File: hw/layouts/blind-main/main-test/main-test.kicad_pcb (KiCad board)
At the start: 2 copper layers, 191 parts

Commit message: Place compact controller and capture split battery carriers
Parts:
- added D6: , blind-control-io:SOT-553-5_L1.6-W1.2-P0.50-LS1.6-TL-1, F.Cu at (135.8, 130.5)
- added J2: , blind-harness:CONN-SMD_4P-P1.25_53261-0471, F.Cu at (140.0, 131.5)
- added J3: , blind-harness:CONN-TH_532610371, F.Cu at (130.5, 123.0)
- added TP1: , blind-pack-features:WirePad18, F.Cu at (142.0, 140.5)
- added TP2: , blind-pack-features:WirePad18, F.Cu at (148.0, 140.5)
- moved C45 1303.6 mm to (112.6, 127.2)
- moved C44 1294.7 mm to (112.3, 134.6)
- moved C41 1282.3 mm to (105.0, 137.0)
- moved C43 1280.6 mm to (116.5, 135.5), turned to 90 degrees
- moved C40 1260.9 mm to (116.0, 132.0)
- moved C42 1253.8 mm to (112.9, 129.3)
- moved L2 1250.0 mm to (107.0, 132.0)
- moved C46 1238.5 mm to (109.0, 135.5)
- moved R46 1227.8 mm to (108.9, 128.5)
- moved R45 1221.1 mm to (105.5, 127.0)
- moved R44 1212.7 mm to (104.2, 128.5)
- moved U9 1195.3 mm to (112.0, 132.0)
- moved C2 1163.4 mm to (137.3, 157.2), turned to 90 degrees
- moved C1 1156.1 mm to (134.6, 157.2), turned to 90 degrees
- moved C21 1131.4 mm to (147.9, 145.1), turned to 90 degrees
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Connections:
- net encoder_a_raw renamed channel_a
- net encoder_b_raw renamed channel_b
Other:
- board outline added: 54 x 71 mm
- copper layers 2 -> 4
- board text added: "SB-C1 R0"

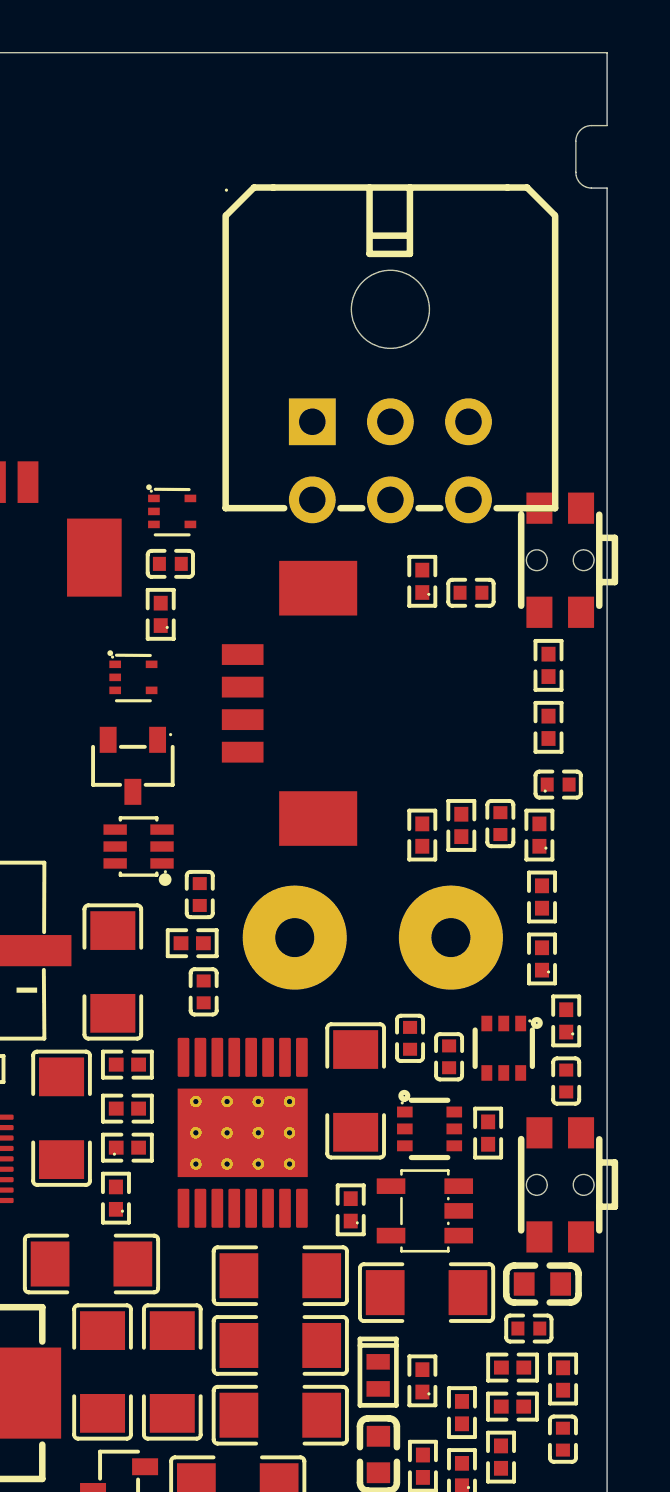
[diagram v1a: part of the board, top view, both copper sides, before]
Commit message: Coordinate retained enclosure and PCB clearance repair checkpoint
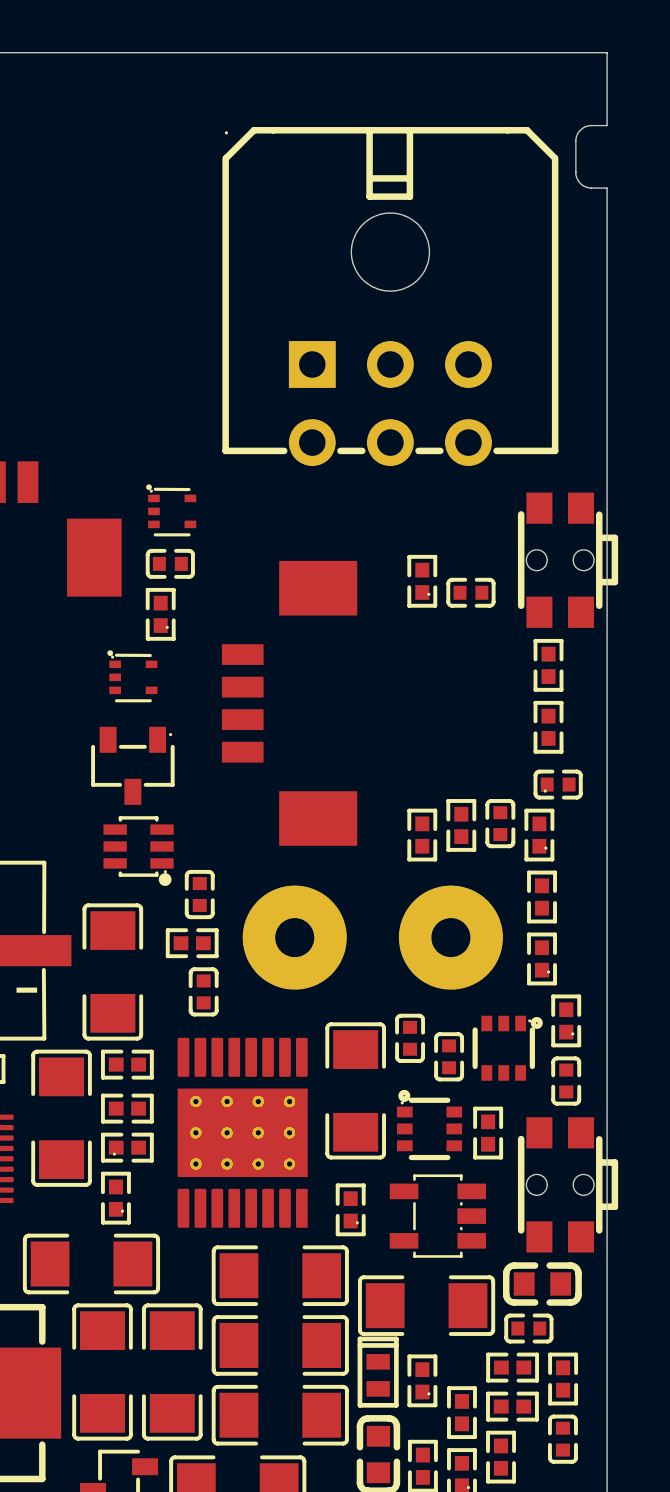
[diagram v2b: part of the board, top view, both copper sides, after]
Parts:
- moved J1 2.20 mm to (145.7, 120.0)
- moved U13 0.54 mm to (147.5, 151.2)
- moved C54 0.50 mm to (147.1, 154.6)

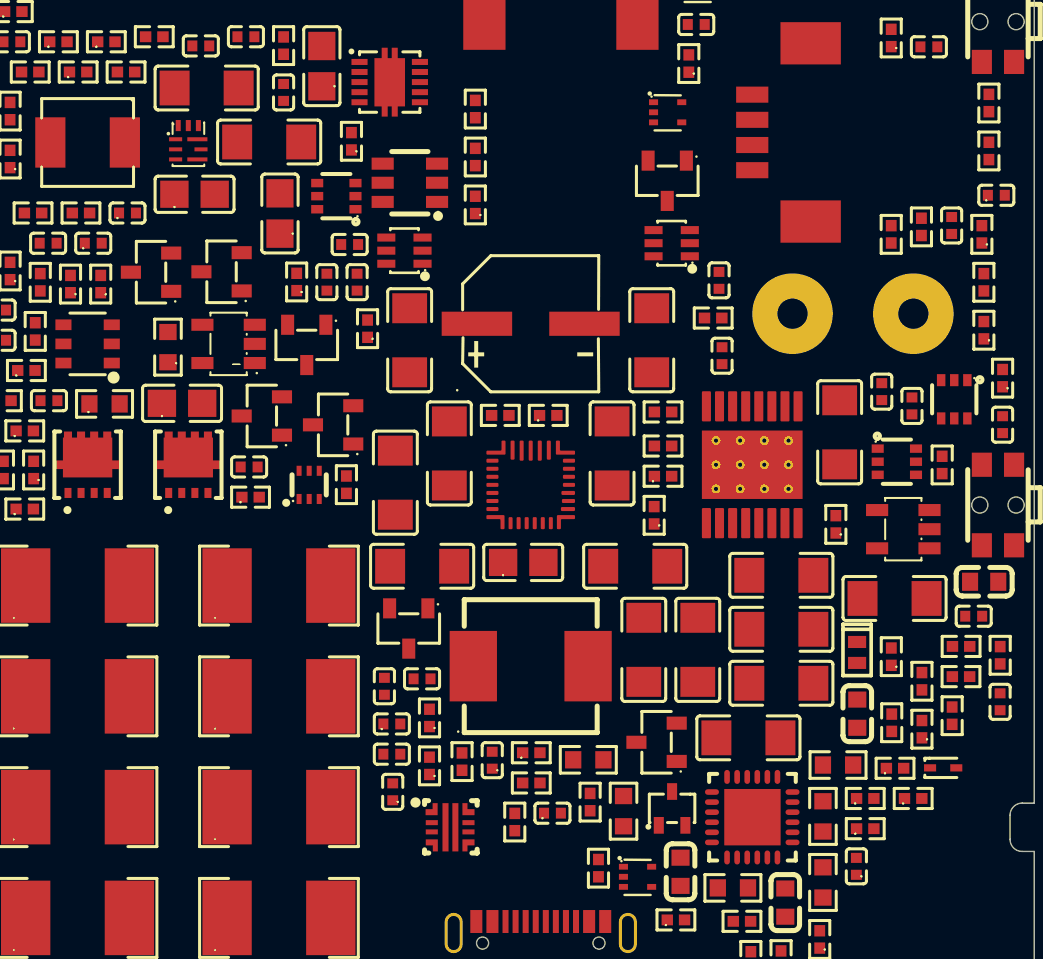
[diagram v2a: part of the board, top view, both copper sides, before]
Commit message: Fix inherited package clearances and repack all three boards
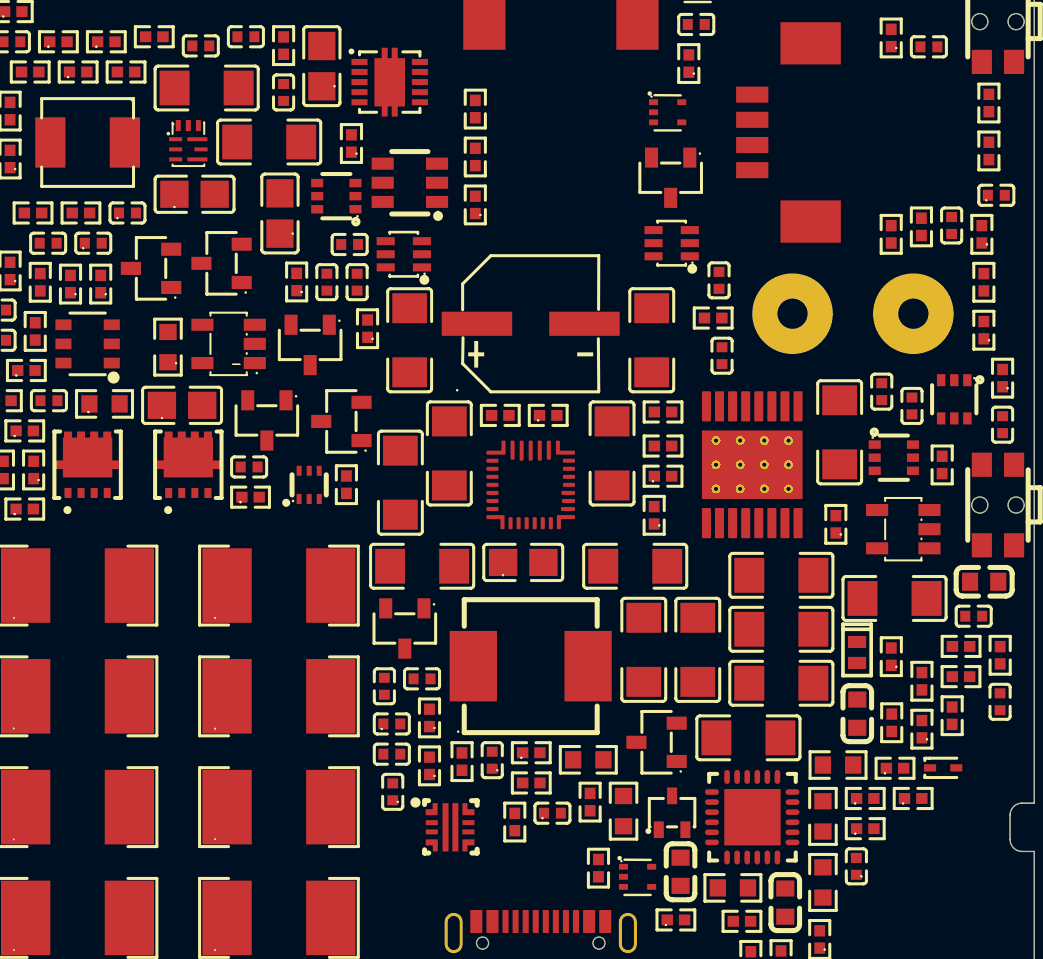
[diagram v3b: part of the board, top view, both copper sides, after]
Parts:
- moved Q2 0.44 mm to (119.6, 145.8)
- moved Q8 0.42 mm to (113.7, 138.0)
- moved Q4 0.33 mm to (115.9, 145.8), turned to 90 degrees
- moved C7 0.25 mm to (122.5, 148.9)
- moved U12 0.25 mm to (147.0, 147.7)
- moved Q10 0.23 mm to (135.9, 133.8)
- moved D4 0.22 mm to (136.0, 165.3)
- moved Q1 0.19 mm to (122.8, 156.1)
- moved Q5 0.19 mm to (110.2, 138.2)
- moved U14 0.18 mm to (122.7, 137.6)
- moved Q7 0.17 mm to (118.0, 142.1)
- moved R17 0.11 mm to (120.1, 132.1)
- moved C39 0.10 mm to (111.7, 145.1)

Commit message: Wire monitored USB power into the circuit and owned sensor runtime
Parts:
- removed R64: , blind-control-io:R0402
- added C61: , SAMSUNG_CL10A105KB8NNNC:C0603, F.Cu at (138.0, 172.0)
- R63: footprint blind-control-io:R0402 -> UNI_ROYAL_0402WGF1002TCE:R0402
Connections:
- C23 pad 1: rail-hv -> host_logic-hv
- C25 pad 1: rail-hv -> host_logic-hv
- C26 pad 1: rail-hv -> host_logic-hv
- C28 pad 1: rail-hv -> host_logic-hv
- C43 pad 1: rail-hv -> host_logic-hv
- C44 pad 1: rail-hv -> host_logic-hv
- C45 pad 1: rail-hv -> host_logic-hv
- C52 pad 1: rail-hv -> host_logic-hv
- C56 pad 1: rail-hv -> host_logic-hv
- C57 pad 1: rail-hv -> host_logic-hv
- C58 pad 1: rail-hv -> host_logic-hv
- C60 pad 1: rail-hv -> host_logic-hv
- J1 pad 3: pack_sda -> SDA
- J1 pad 4: pack_scl -> SCL
- L2 pad 2: rail-hv -> host_logic-hv
- Q2 pad 2: rail-hv -> host_logic-hv
- R19 pad 1: rail-hv -> host_logic-hv
- R20 pad 1: rail-hv -> host_logic-hv
- R22 pad 1: rail-hv -> host_logic-hv
- R24 pad 1: rail-hv -> host_logic-hv
- R26 pad 1: rail-hv -> host_logic-hv
- R27 pad 1: rail-hv -> host_logic-hv
- R27 pad 2: pack_scl -> SCL
- R28 pad 1: rail-hv -> host_logic-hv
- R28 pad 2: pack_sda -> SDA
- R29 pad 1: rail-hv -> host_logic-hv
- R30 pad 1: rail-hv -> host_logic-hv
- R32 pad 1: rail-hv -> host_logic-hv
- R35 pad 1: rail-hv -> host_logic-hv
- R36 pad 1: rail-hv -> host_logic-hv
- R46 pad 1: rail-hv -> host_logic-hv
- R63 pad 1: SCL -> host_logic-hv
- R63 pad 2: lv -> ALERT
- R7 pad 2: rail-hv -> host_logic-hv
- R89 pad 1: rail-hv -> host_logic-hv
- R90 pad 1: rail-hv -> host_logic-hv
- R92 pad 1: rail-hv -> host_logic-hv
- R93 pad 1: rail-hv -> host_logic-hv
- U1 pad 14: pack_scl -> SCL
- U1 pad 15: pack_sda -> SDA
- U1 pad 21: INT_n -> ALERT
- U11 pad 22: lv -> host_logic-hv
- U12 pad 5: rail-hv -> host_logic-hv
- U14 pad 5: rail-hv -> host_logic-hv
- U15 pad 5: rail-hv -> host_logic-hv
- U15 pad 6: rail-hv -> host_logic-hv
- U16 pad 1: rail-hv -> host_logic-hv
- U16 pad 10: rail-hv -> host_logic-hv
- U17 pad 5: rail-hv -> host_logic-hv
- U2 pad 5: rail-hv -> host_logic-hv
- U3 pad 11: pack_sda -> SDA
- U3 pad 12: pack_scl -> SCL
- U3 pad 2: rail-hv -> host_logic-hv
- U3 pad 24: INT_n -> ALERT
- U8 pad 5: rail-hv -> host_logic-hv
- U9 pad 3: rail-hv -> host_logic-hv

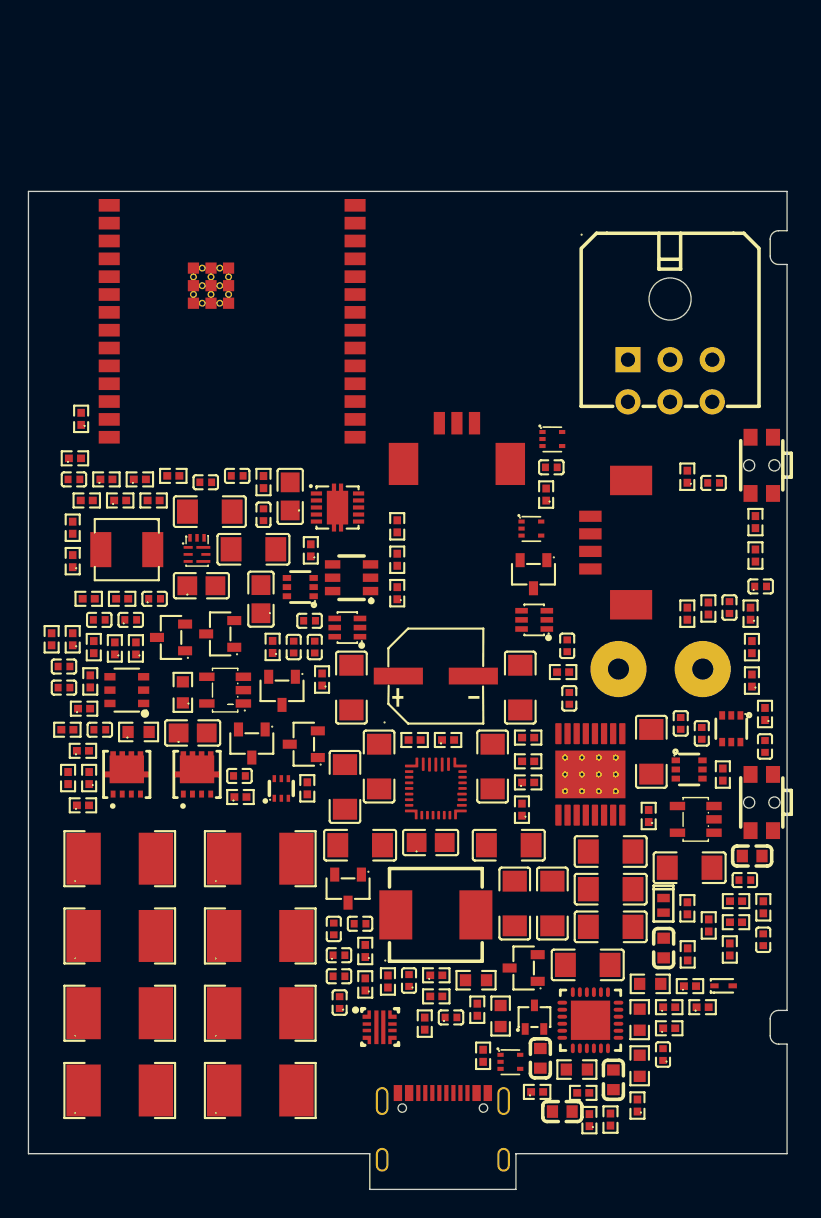
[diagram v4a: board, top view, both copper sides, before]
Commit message: Make the cleaner controller reproducible from circuit source (#3)
* Rebuild cleaner controller from circuit source and verify native previews

* Use compiler-compatible Python without changing native render runtime
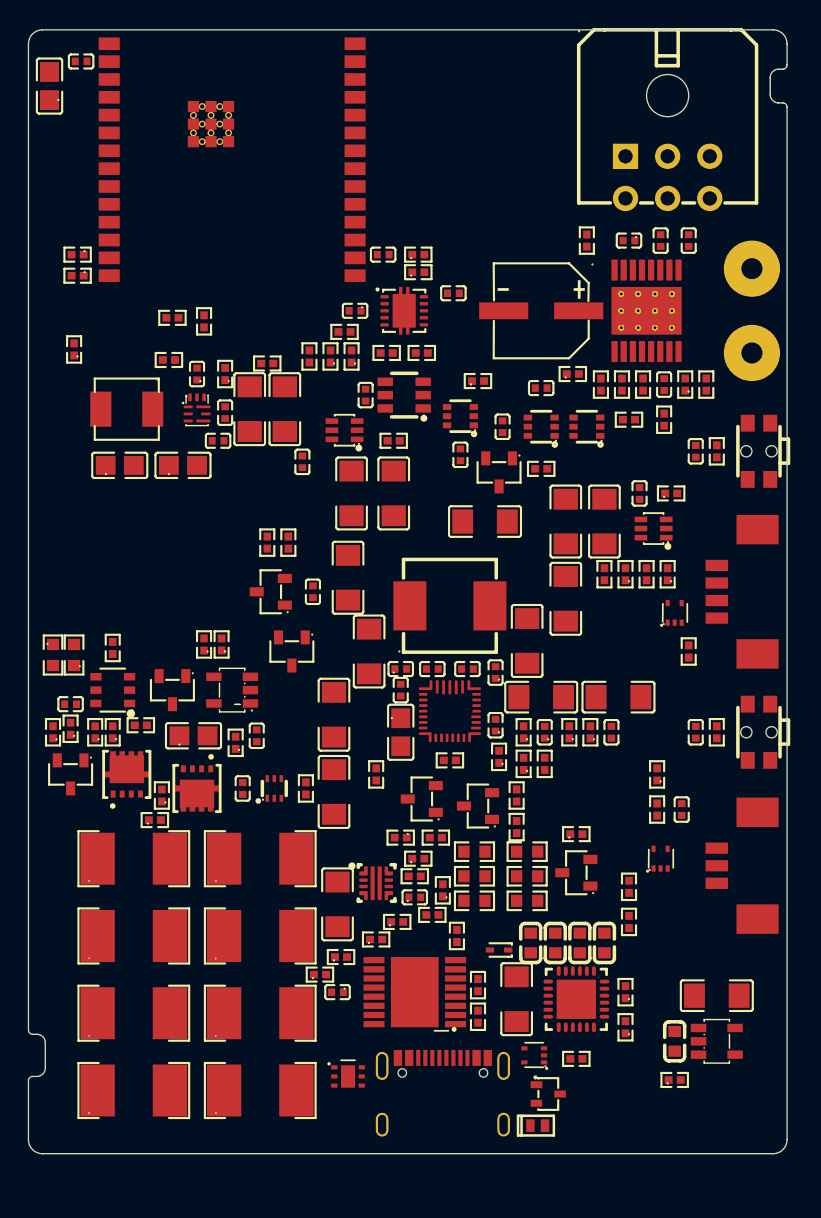
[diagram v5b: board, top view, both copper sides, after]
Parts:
- added C62: , blind-power:C0402, F.Cu at (122.0, 163.5)
- added C63: , blind-usb:C1206, F.Cu at (122.0, 157.2)
- added R64: , blind-core:R0402, F.Cu at (122.2, 161.0)
- added R94: , blind-usb-protection:R0402, F.Cu at (130.5, 159.5)
- added R95: , blind-usb-protection:R0402, F.Cu at (132.0, 163.0)
- added R96: , UNI_ROYAL_0402WGF3903TCE:R0402, F.Cu at (132.0, 165.2)
- added R97: , blind-control-io:R0402, F.Cu at (120.8, 162.2)
- added R98: , blind-control-io:R0402, F.Cu at (124.8, 159.8)
- added U18: , blind-usb-protection:TPS26600_PWP16, F.Cu at (127.5, 163.5)
- added U19: , blind-usb-protection:TVS1800_DRV6, F.Cu at (122.8, 169.5)
- moved R38 40.7 mm to (143.8, 120.2)
- moved R34 39.1 mm to (142.2, 120.2), turned to 90 degrees
- moved R33 39.0 mm to (140.8, 120.2)
- moved C52 36.6 mm to (133.8, 123.2), turned to 90 degrees
- moved J3 36.5 mm to (149.0, 154.5), turned to 90 degrees
- moved R36 35.1 mm to (142.8, 122.8)
- moved C30 35.1 mm to (147.5, 125.0)
- moved R20 34.8 mm to (120.0, 118.2)
- moved C35 34.4 mm to (145.0, 110.0)
- moved C25 33.9 mm to (101.5, 99.0)
- moved C33 33.7 mm to (147.0, 110.0)
- moved U4 33.2 mm to (144.0, 115.0)
- moved R63 33.0 mm to (136.5, 126.2), turned to 0 degrees
- moved C26 31.5 mm to (103.8, 97.2), turned to 180 degrees
- moved R35 31.2 mm to (139.8, 110.0)
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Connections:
- net DVDT renamed usb-DVDT
- net usb-2 renamed usb-2-1
- D3 pad 2: raw-hv -> guarded-hv
- Q3 pad 2: raw-hv -> guarded-hv
- R51 pad 1: raw-hv -> guarded-hv
- R57 pad 1: raw-hv -> guarded-hv
- R59 pad 1: raw-hv -> guarded-hv
- U10 pad 5: raw-hv -> guarded-hv
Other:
- board size 54 x 71 mm -> 54 x 80 mm
- board text removed: "SB-C1 R0"
